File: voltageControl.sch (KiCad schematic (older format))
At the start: 5 parts

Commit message: updated with association labels
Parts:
- added C302: 100nF, symbol C
- R301: renamed from R?; value R -> 19.1K
- R302: renamed from R?; value R -> 2.2k
- gave numbers to parts that had none: 3
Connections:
- wire segments 16 -> 18
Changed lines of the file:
@@
 $EndDescr
 $Comp
-L GND #PWR?
+L GND #PWR305
 U 1 1 5521C966
 P 4500 4800
-F 0 "#PWR?" H 4500 4550 60  0001 C CNN
-F 1 "GND" H 4500 4650 60  0000 C CNN
-F 2 "" H 4500 4800 60  0000 C CNN
-F 3 "" H 4500 4800 60  0000 C CNN
-	1    4500 4800
-	1    0    0    -1
-$EndComp
-$Comp
-L GND #PWR?
+F 0 "#PWR305" H 4500 4550 60  0001 C CNN
+F 1 "GND" H 4500 4650 60  0000 C CNN
+F 2 "" H 4500 4800 60  0000 C CNN
+F 3 "" H 4500 4800 60  0000 C CNN
+	1    4500 4800
+	1    0    0    -1
+$EndComp
+$Comp
+L GND #PWR301
 U 1 1 5521C96C
 P 3700 3900
-F 0 "#PWR?" H 3700 3650 60  0001 C CNN
-F 1 "GND" H 3700 3750 60  0000 C CNN
-F 2 "" H 3700 3900 60  0000 C CNN
-F 3 "" H 3700 3900 60  0000 C CNN
-	1    3700 3900
-	1    0    0    -1
-$EndComp
-$Comp
-L GND #PWR?
+F 0 "#PWR301" H 3700 3650 60  0001 C CNN
+F 1 "GND" H 3700 3750 60  0000 C CNN
+F 2 "" H 3700 3900 60  0000 C CNN
+F 3 "" H 3700 3900 60  0000 C CNN
+	1    3700 3900
+	1    0    0    -1
+$EndComp
+$Comp
+L GND #PWR306
 U 1 1 5521C972
 P 4500 4800
-F 0 "#PWR?" H 4500 4550 60  0001 C CNN
-F 1 "GND" H 4500 4650 60  0000 C CNN
-F 2 "" H 4500 4800 60  0000 C CNN
-F 3 "" H 4500 4800 60  0000 C CNN
-	1    4500 4800
-	1    0    0    -1
-$EndComp
-$Comp
-L GND #PWR?
+F 0 "#PWR306" H 4500 4550 60  0001 C CNN
+F 1 "GND" H 4500 4650 60  0000 C CNN
+F 2 "" H 4500 4800 60  0000 C CNN
+F 3 "" H 4500 4800 60  0000 C CNN
+	1    4500 4800
+	1    0    0    -1
+$EndComp
+$Comp
+L GND #PWR302
 U 1 1 5521C978
 P 3700 3900
-F 0 "#PWR?" H 3700 3650 60  0001 C CNN
+F 0 "#PWR302" H 3700 3650 60  0001 C CNN
 F 1 "GND" H 3700 3750 60  0000 C CNN
 F 2 "" H 3700 3900 60  0000 C CNN
@@
 	4500 4700 4500 4800
 $Comp
-L GND #PWR?
+L GND #PWR307
 U 1 1 5521C982
 P 4500 4800
-F 0 "#PWR?" H 4500 4550 60  0001 C CNN
-F 1 "GND" H 4500 4650 60  0000 C CNN
-F 2 "" H 4500 4800 60  0000 C CNN
-F 3 "" H 4500 4800 60  0000 C CNN
-	1    4500 4800
-	1    0    0    -1
-$EndComp
-$Comp
-L GND #PWR?
+F 0 "#PWR307" H 4500 4550 60  0001 C CNN
+F 1 "GND" H 4500 4650 60  0000 C CNN
+F 2 "" H 4500 4800 60  0000 C CNN
+F 3 "" H 4500 4800 60  0000 C CNN
+	1    4500 4800
+	1    0    0    -1
+$EndComp
+$Comp
+L GND #PWR303
 U 1 1 5521C988
 P 3700 3900
-F 0 "#PWR?" H 3700 3650 60  0001 C CNN
-F 1 "GND" H 3700 3750 60  0000 C CNN
-F 2 "" H 3700 3900 60  0000 C CNN
-F 3 "" H 3700 3900 60  0000 C CNN
-	1    3700 3900
-	1    0    0    -1
-$EndComp
-$Comp
-L LMV358 U?
+F 0 "#PWR303" H 3700 3650 60  0001 C CNN
+F 1 "GND" H 3700 3750 60  0000 C CNN
+F 2 "" H 3700 3900 60  0000 C CNN
+F 3 "" H 3700 3900 60  0000 C CNN
+	1    3700 3900
+	1    0    0    -1
+$EndComp
+$Comp
+L LMV358 U201
 U 2 1 5521C98E
 P 4600 4300
-F 0 "U?" H 4550 4500 60  0000 L CNN
+F 0 "U201" H 4550 4500 60  0000 L CNN
 F 1 "LMV358" H 4550 4050 60  0000 L CNN
 F 2 "" H 4600 4300 60  0000 C CNN
@@
 $EndComp
 $Comp
-L GND #PWR?
+L GND #PWR308
 U 1 1 5521C995
 P 4500 4800
-F 0 "#PWR?" H 4500 4550 60  0001 C CNN
-F 1 "GND" H 4500 4650 60  0000 C CNN
-F 2 "" H 4500 4800 60  0000 C CNN
-F 3 "" H 4500 4800 60  0000 C CNN
-	1    4500 4800
-	1    0    0    -1
-$EndComp
-$Comp
-L C C?
+F 0 "#PWR308" H 4500 4550 60  0001 C CNN
+F 1 "GND" H 4500 4650 60  0000 C CNN
+F 2 "" H 4500 4800 60  0000 C CNN
+F 3 "" H 4500 4800 60  0000 C CNN
+	1    4500 4800
+	1    0    0    -1
+$EndComp
+$Comp
+L C C301
 U 1 1 5521C99B
 P 3700 3600
-F 0 "C?" H 3750 3700 50  0000 L CNN
+F 0 "C301" H 3750 3700 50  0000 L CNN
 F 1 "C" H 3750 3500 50  0000 L CNN
 F 2 "" H 3738 3450 30  0000 C CNN
@@
 $EndComp
 $Comp
-L GND #PWR?
+L GND #PWR304
 U 1 1 5521C9A2
 P 3700 3900
-F 0 "#PWR?" H 3700 3650 60  0001 C CNN
+F 0 "#PWR304" H 3700 3650 60  0001 C CNN
 F 1 "GND" H 3700 3750 60  0000 C CNN
 F 2 "" H 3700 3900 60  0000 C CNN
@@
 	5100 4300 5750 4300
 $Comp
-L DIODE D?
+L DIODE D301
 U 1 1 5521CA2B
 P 5950 4300
-F 0 "D?" H 5950 4400 50  0000 C CNN
+F 0 "D301" H 5950 4400 50  0000 C CNN
 F 1 "DIODE" H 5950 4200 50  0000 C CNN
 F 2 "" H 5950 4300 60  0000 C CNN
@@
 $EndComp
 $Comp
-L R R?
+L R R301
 U 1 1 5521CAB7
 P 7300 4900
-F 0 "R?" V 7380 4900 50  0000 C CNN
-F 1 "R" V 7307 4901 50  0000 C CNN
+F 0 "R301" V 7380 4900 50  0000 C CNN
+F 1 "19.1K" V 7307 4901 50  0000 C CNN
 F 2 "" V 7230 4900 30  0000 C CNN
 F 3 "" H 7300 4900 30  0000 C CNN
@@
 $EndComp
 $Comp
-L R R?
+L R R302
 U 1 1 5521CAFE
 P 7300 5750
-F 0 "R?" V 7380 5750 50  0000 C CNN
-F 1 "R" V 7307 5751 50  0000 C CNN
+F 0 "R302" V 7380 5750 50  0000 C CNN
+F 1 "2.2k" V 7307 5751 50  0000 C CNN
 F 2 "" V 7230 5750 30  0000 C CNN
 F 3 "" H 7300 5750 30  0000 C CNN
@@
 Wire Wire Line
 	7300 4500 7950 4500
-Text HLabel 7950 6100 2    60   Input ~ 0
+Text HLabel 8000 6250 2    60   Input ~ 0
 Current_Sink-
 Wire Wire Line
-	7300 6000 7300 6100
-Wire Wire Line
-	7300 6100 7950 6100
+	7300 6000 7300 6250
 Text HLabel 2350 4200 0    60   Input ~ 0
 DAC_Va
 Text HLabel 8000 5300 2    60   Output ~ 0
 VoltageRead
+$Comp
+L C C302
+U 1 1 55220BE7
+P 7700 5700
+F 0 "C302" H 7750 5800 50  0000 L CNN
+F 1 "100nF" H 7750 5600 50  0000 L CNN
+F 2 "" H 7738 5550 30  0000 C CNN
+F 3 "" H 7700 5700 60  0000 C CNN
+F 4 "Value" H 7700 5700 60  0001 C CNN "MPN"
+	1    7700 5700
+	1    0    0    -1
+$EndComp
+$Comp
+L GND #PWR309
+U 1 1 55220C0E
+P 7700 5950
+F 0 "#PWR309" H 7700 5700 60  0001 C CNN
+F 1 "GND" H 7700 5800 60  0000 C CNN
+F 2 "" H 7700 5950 60  0000 C CNN
+F 3 "" H 7700 5950 60  0000 C CNN
+	1    7700 5950
+	1    0    0    -1
+$EndComp
+Wire Wire Line
+	7300 6250 8000 6250
+Wire Wire Line
+	7700 5900 7700 5950
+Wire Wire Line
+	7700 5500 7700 5300
+Connection ~ 7700 5300
 $EndSCHEMATC

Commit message: updated schematic with corrected wiring after all passives became disconnected
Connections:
- wire segments 18 -> 19
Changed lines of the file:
@@
 	4100 4400 4100 5300
 Wire Wire Line
-	3700 3800 3700 3900
+	3700 3750 3700 3900
 Wire Wire Line
 	4500 4700 4500 4800
@@
 $EndComp
 Wire Wire Line
-	7300 5150 7300 5500
+	7300 5050 7300 5600
 Connection ~ 7300 5300
 Text HLabel 7950 4300 2    60   Output ~ 0
@@
 Current_Sink+
 Wire Wire Line
-	7300 4650 7300 4500
+	7300 4500 7300 4750
 Wire Wire Line
 	7300 4500 7950 4500
@@
 Current_Sink-
 Wire Wire Line
-	7300 6000 7300 6250
+	7300 5900 7300 6250
 Text HLabel 2350 4200 0    60   Input ~ 0
 DAC_Va
@@
 	7300 6250 8000 6250
 Wire Wire Line
-	7700 5900 7700 5950
+	7700 5850 7700 5950
 Wire Wire Line
-	7700 5500 7700 5300
+	7700 5300 7700 5550
 Connection ~ 7700 5300
+Wire Wire Line
+	3700 3450 3700 3400
+Connection ~ 3700 3400
 $EndSCHEMATC

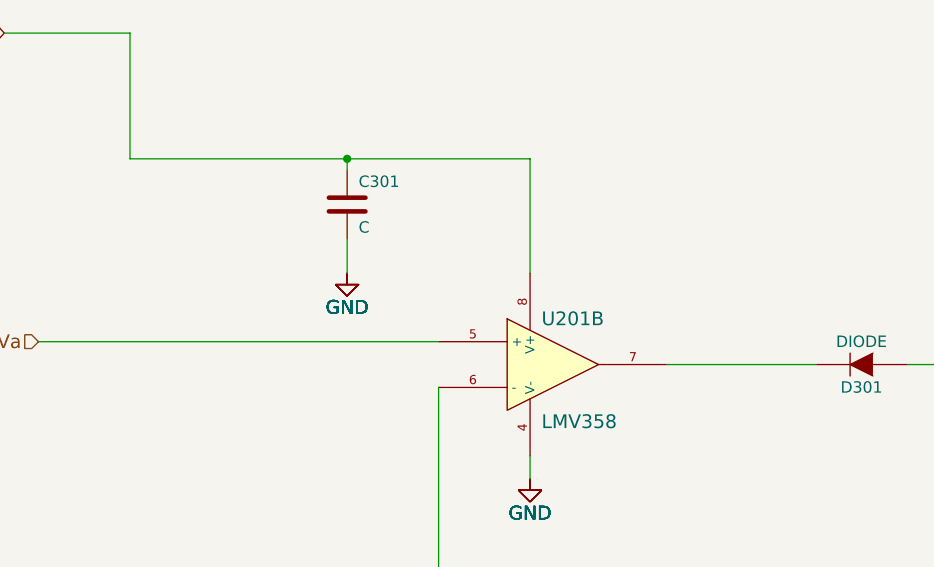
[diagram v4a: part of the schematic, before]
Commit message: updated project with most footprint associations
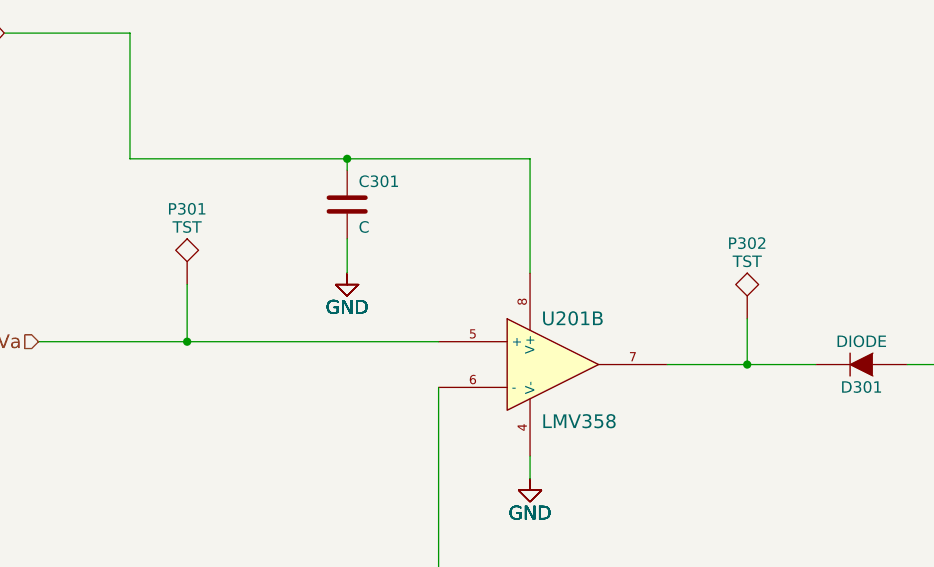
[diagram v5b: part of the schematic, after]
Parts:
- added P301, P302: TST, symbol TST
- C301, C302: footprint (none) -> Capacitors_SMD:C_0805_HandSoldering
- R301, R302: footprint (none) -> Resistors_SMD:R_0805_HandSoldering
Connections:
- net DAC_Va: now also P301.1
- net at D301.2 (K), U201.7: now also P302.1
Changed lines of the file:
@@
 $EndDescr
 $Comp
-L GND #PWR013
+L GND #PWR305
 U 1 1 5521C966
 P 4500 4800
-F 0 "#PWR013" H 4500 4550 60  0001 C CNN
-F 1 "GND" H 4500 4650 60  0000 C CNN
-F 2 "" H 4500 4800 60  0000 C CNN
-F 3 "" H 4500 4800 60  0000 C CNN
-	1    4500 4800
-	1    0    0    -1
-$EndComp
-$Comp
-L GND #PWR014
+F 0 "#PWR305" H 4500 4550 60  0001 C CNN
+F 1 "GND" H 4500 4650 60  0000 C CNN
+F 2 "" H 4500 4800 60  0000 C CNN
+F 3 "" H 4500 4800 60  0000 C CNN
+	1    4500 4800
+	1    0    0    -1
+$EndComp
+$Comp
+L GND #PWR301
 U 1 1 5521C96C
 P 3700 3900
-F 0 "#PWR014" H 3700 3650 60  0001 C CNN
-F 1 "GND" H 3700 3750 60  0000 C CNN
-F 2 "" H 3700 3900 60  0000 C CNN
-F 3 "" H 3700 3900 60  0000 C CNN
-	1    3700 3900
-	1    0    0    -1
-$EndComp
-$Comp
-L GND #PWR015
+F 0 "#PWR301" H 3700 3650 60  0001 C CNN
+F 1 "GND" H 3700 3750 60  0000 C CNN
+F 2 "" H 3700 3900 60  0000 C CNN
+F 3 "" H 3700 3900 60  0000 C CNN
+	1    3700 3900
+	1    0    0    -1
+$EndComp
+$Comp
+L GND #PWR306
 U 1 1 5521C972
 P 4500 4800
-F 0 "#PWR015" H 4500 4550 60  0001 C CNN
-F 1 "GND" H 4500 4650 60  0000 C CNN
-F 2 "" H 4500 4800 60  0000 C CNN
-F 3 "" H 4500 4800 60  0000 C CNN
-	1    4500 4800
-	1    0    0    -1
-$EndComp
-$Comp
-L GND #PWR016
+F 0 "#PWR306" H 4500 4550 60  0001 C CNN
+F 1 "GND" H 4500 4650 60  0000 C CNN
+F 2 "" H 4500 4800 60  0000 C CNN
+F 3 "" H 4500 4800 60  0000 C CNN
+	1    4500 4800
+	1    0    0    -1
+$EndComp
+$Comp
+L GND #PWR302
 U 1 1 5521C978
 P 3700 3900
-F 0 "#PWR016" H 3700 3650 60  0001 C CNN
-F 1 "GND" H 3700 3750 60  0000 C CNN
-F 2 "" H 3700 3900 60  0000 C CNN
-F 3 "" H 3700 3900 60  0000 C CNN
-	1    3700 3900
-	1    0    0    -1
-$EndComp
-Wire Wire Line
-	4100 5300 8000 5300
-Wire Wire Line
-	4100 4400 4100 5300
-Wire Wire Line
-	3700 3750 3700 3900
-Wire Wire Line
-	4500 4700 4500 4800
-$Comp
-L GND #PWR017
+F 0 "#PWR302" H 3700 3650 60  0001 C CNN
+F 1 "GND" H 3700 3750 60  0000 C CNN
+F 2 "" H 3700 3900 60  0000 C CNN
+F 3 "" H 3700 3900 60  0000 C CNN
+	1    3700 3900
+	1    0    0    -1
+$EndComp
+$Comp
+L GND #PWR307
 U 1 1 5521C982
 P 4500 4800
-F 0 "#PWR017" H 4500 4550 60  0001 C CNN
-F 1 "GND" H 4500 4650 60  0000 C CNN
-F 2 "" H 4500 4800 60  0000 C CNN
-F 3 "" H 4500 4800 60  0000 C CNN
-	1    4500 4800
-	1    0    0    -1
-$EndComp
-$Comp
-L GND #PWR018
+F 0 "#PWR307" H 4500 4550 60  0001 C CNN
+F 1 "GND" H 4500 4650 60  0000 C CNN
+F 2 "" H 4500 4800 60  0000 C CNN
+F 3 "" H 4500 4800 60  0000 C CNN
+	1    4500 4800
+	1    0    0    -1
+$EndComp
+$Comp
+L GND #PWR303
 U 1 1 5521C988
 P 3700 3900
-F 0 "#PWR018" H 3700 3650 60  0001 C CNN
+F 0 "#PWR303" H 3700 3650 60  0001 C CNN
 F 1 "GND" H 3700 3750 60  0000 C CNN
 F 2 "" H 3700 3900 60  0000 C CNN
@@
 F 0 "U201" H 4550 4500 60  0000 L CNN
 F 1 "LMV358" H 4550 4050 60  0000 L CNN
-F 2 "" H 4600 4300 60  0000 C CNN
+F 2 "" H 4600 4300 60  0001 C CNN
 F 3 "" H 4600 4300 60  0000 C CNN
 	2    4600 4300
@@
 $EndComp
 $Comp
-L GND #PWR019
+L GND #PWR308
 U 1 1 5521C995
 P 4500 4800
-F 0 "#PWR019" H 4500 4550 60  0001 C CNN
+F 0 "#PWR308" H 4500 4550 60  0001 C CNN
 F 1 "GND" H 4500 4650 60  0000 C CNN
 F 2 "" H 4500 4800 60  0000 C CNN
@@
 F 0 "C301" H 3750 3700 50  0000 L CNN
 F 1 "C" H 3750 3500 50  0000 L CNN
-F 2 "" H 3738 3450 30  0000 C CNN
+F 2 "Capacitors_SMD:C_0805_HandSoldering" H 3738 3450 30  0001 C CNN
 F 3 "" H 3700 3600 60  0000 C CNN
 	1    3700 3600
@@
 $EndComp
 $Comp
-L GND #PWR020
+L GND #PWR304
 U 1 1 5521C9A2
 P 3700 3900
-F 0 "#PWR020" H 3700 3650 60  0001 C CNN
+F 0 "#PWR304" H 3700 3650 60  0001 C CNN
 F 1 "GND" H 3700 3750 60  0000 C CNN
 F 2 "" H 3700 3900 60  0000 C CNN
@@
 Text GLabel 2200 2850 0    60   Input ~ 0
 2.7V
-Wire Wire Line
-	4500 3900 4500 3400
-Wire Wire Line
-	4500 3400 2750 3400
-Wire Wire Line
-	2750 3400 2750 2850
-Wire Wire Line
-	2750 2850 2200 2850
-Wire Wire Line
-	2350 4200 4100 4200
-Wire Wire Line
-	5100 4300 5750 4300
 $Comp
 L DIODE D301
@@
 F 0 "D301" H 5950 4400 50  0000 C CNN
 F 1 "DIODE" H 5950 4200 50  0000 C CNN
-F 2 "" H 5950 4300 60  0000 C CNN
+F 2 "" H 5950 4300 60  0001 C CNN
 F 3 "" H 5950 4300 60  0000 C CNN
 	1    5950 4300
@@
 F 0 "R301" V 7380 4900 50  0000 C CNN
 F 1 "19.1K" V 7307 4901 50  0000 C CNN
-F 2 "" V 7230 4900 30  0000 C CNN
+F 2 "Resistors_SMD:R_0805_HandSoldering" V 7230 4900 30  0001 C CNN
 F 3 "" H 7300 4900 30  0000 C CNN
 	1    7300 4900
@@
 F 0 "R302" V 7380 5750 50  0000 C CNN
 F 1 "2.2k" V 7307 5751 50  0000 C CNN
-F 2 "" V 7230 5750 30  0000 C CNN
+F 2 "Resistors_SMD:R_0805_HandSoldering" V 7230 5750 30  0001 C CNN
 F 3 "" H 7300 5750 30  0000 C CNN
 	1    7300 5750
 	1    0    0    -1
 $EndComp
-Wire Wire Line
-	7300 5050 7300 5600
-Connection ~ 7300 5300
 Text HLabel 7950 4300 2    60   Output ~ 0
 Vcontrol
-Wire Wire Line
-	6150 4300 7950 4300
 Text HLabel 7950 4500 2    60   Input ~ 0
 Current_Sink+
-Wire Wire Line
-	7300 4500 7300 4750
-Wire Wire Line
-	7300 4500 7950 4500
 Text HLabel 8000 6250 2    60   Input ~ 0
 Current_Sink-
-Wire Wire Line
-	7300 5900 7300 6250
 Text HLabel 2350 4200 0    60   Input ~ 0
 DAC_Va
@@
 F 0 "C302" H 7750 5800 50  0000 L CNN
 F 1 "100nF" H 7750 5600 50  0000 L CNN
-F 2 "" H 7738 5550 30  0000 C CNN
+F 2 "Capacitors_SMD:C_0805_HandSoldering" H 7738 5550 30  0001 C CNN
 F 3 "" H 7700 5700 60  0000 C CNN
 F 4 "Value" H 7700 5700 60  0001 C CNN "MPN"
@@
 $EndComp
 $Comp
-L GND #PWR021
+L GND #PWR309
 U 1 1 55220C0E
 P 7700 5950
-F 0 "#PWR021" H 7700 5700 60  0001 C CNN
+F 0 "#PWR309" H 7700 5700 60  0001 C CNN
 F 1 "GND" H 7700 5800 60  0000 C CNN
 F 2 "" H 7700 5950 60  0000 C CNN
@@
 	1    0    0    -1
 $EndComp
+$Comp
+L TST P301
+U 1 1 5528F0BE
+P 3000 3950
+F 0 "P301" H 3000 4250 50  0000 C BNN
+F 1 "TST" H 3000 4200 50  0000 C CNN
+F 2 "" H 3000 3950 60  0000 C CNN
+F 3 "" H 3000 3950 60  0000 C CNN
+	1    3000 3950
+	1    0    0    -1
+$EndComp
+Wire Wire Line
+	4100 5300 8000 5300
+Wire Wire Line
+	4100 4400 4100 5300
+Wire Wire Line
+	3700 3750 3700 3900
+Wire Wire Line
+	4500 4700 4500 4800
+Wire Wire Line
+	4500 3900 4500 3400
+Wire Wire Line
+	4500 3400 2750 3400
+Wire Wire Line
+	2750 3400 2750 2850
+Wire Wire Line
+	2750 2850 2200 2850
+Wire Wire Line
+	2350 4200 4100 4200
+Wire Wire Line
+	5100 4300 5750 4300
+Wire Wire Line
+	7300 5050 7300 5600
+Connection ~ 7300 5300
+Wire Wire Line
+	6150 4300 7950 4300
+Wire Wire Line
+	7300 4500 7300 4750
+Wire Wire Line
+	7300 4500 7950 4500
+Wire Wire Line
+	7300 5900 7300 6250
 Wire Wire Line
 	7300 6250 8000 6250
@@
 	3700 3450 3700 3400
 Connection ~ 3700 3400
+Wire Wire Line
+	3000 3950 3000 4200
+Connection ~ 3000 4200
+$Comp
+L TST P302
+U 1 1 5528F58F
+P 5450 4100
+F 0 "P302" H 5450 4400 50  0000 C BNN
+F 1 "TST" H 5450 4350 50  0000 C CNN
+F 2 "" H 5450 4100 60  0000 C CNN
+F 3 "" H 5450 4100 60  0000 C CNN
+	1    5450 4100
+	1    0    0    -1
+$EndComp
+Wire Wire Line
+	5450 4100 5450 4300
+Connection ~ 5450 4300
 $EndSCHEMATC

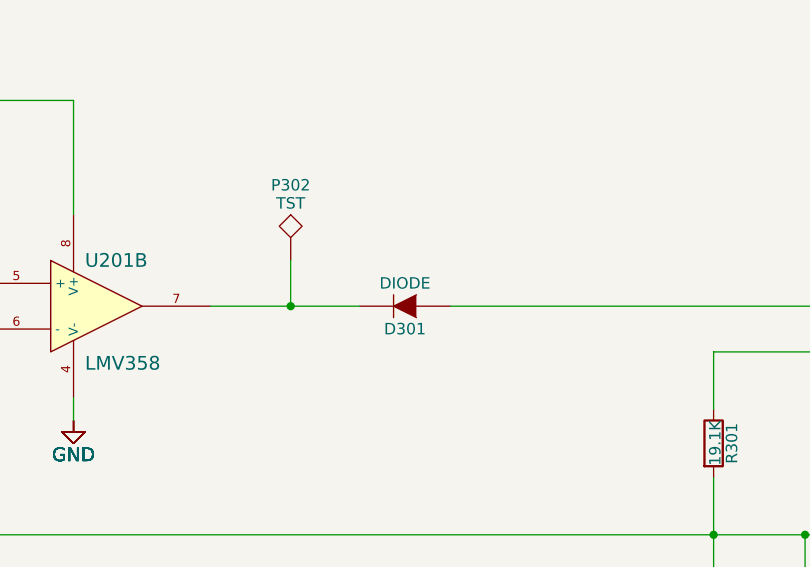
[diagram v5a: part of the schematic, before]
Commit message: association of footprints complete
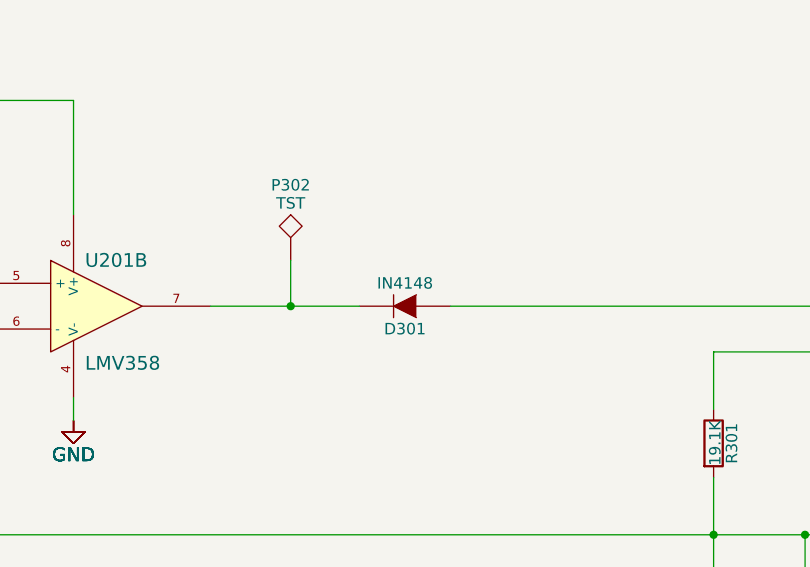
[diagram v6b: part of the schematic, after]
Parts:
- D301: value DIODE -> IN4148; footprint (none) -> SMD_Packages:SOD-523; MPN (none) -> 1N4148WT-7
- P301, P302: footprint (none) -> Measurement_Points:Measurement_Point_Round-TH_Small
- U201: footprint (none) -> SMD_Packages:SOIC-8-N
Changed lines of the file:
@@
 $EndDescr
 $Comp
-L GND #PWR305
+L GND #PWR013
 U 1 1 5521C966
 P 4500 4800
-F 0 "#PWR305" H 4500 4550 60  0001 C CNN
-F 1 "GND" H 4500 4650 60  0000 C CNN
-F 2 "" H 4500 4800 60  0000 C CNN
-F 3 "" H 4500 4800 60  0000 C CNN
-	1    4500 4800
-	1    0    0    -1
-$EndComp
-$Comp
-L GND #PWR301
+F 0 "#PWR013" H 4500 4550 60  0001 C CNN
+F 1 "GND" H 4500 4650 60  0000 C CNN
+F 2 "" H 4500 4800 60  0000 C CNN
+F 3 "" H 4500 4800 60  0000 C CNN
+	1    4500 4800
+	1    0    0    -1
+$EndComp
+$Comp
+L GND #PWR014
 U 1 1 5521C96C
 P 3700 3900
-F 0 "#PWR301" H 3700 3650 60  0001 C CNN
-F 1 "GND" H 3700 3750 60  0000 C CNN
-F 2 "" H 3700 3900 60  0000 C CNN
-F 3 "" H 3700 3900 60  0000 C CNN
-	1    3700 3900
-	1    0    0    -1
-$EndComp
-$Comp
-L GND #PWR306
+F 0 "#PWR014" H 3700 3650 60  0001 C CNN
+F 1 "GND" H 3700 3750 60  0000 C CNN
+F 2 "" H 3700 3900 60  0000 C CNN
+F 3 "" H 3700 3900 60  0000 C CNN
+	1    3700 3900
+	1    0    0    -1
+$EndComp
+$Comp
+L GND #PWR015
 U 1 1 5521C972
 P 4500 4800
-F 0 "#PWR306" H 4500 4550 60  0001 C CNN
-F 1 "GND" H 4500 4650 60  0000 C CNN
-F 2 "" H 4500 4800 60  0000 C CNN
-F 3 "" H 4500 4800 60  0000 C CNN
-	1    4500 4800
-	1    0    0    -1
-$EndComp
-$Comp
-L GND #PWR302
+F 0 "#PWR015" H 4500 4550 60  0001 C CNN
+F 1 "GND" H 4500 4650 60  0000 C CNN
+F 2 "" H 4500 4800 60  0000 C CNN
+F 3 "" H 4500 4800 60  0000 C CNN
+	1    4500 4800
+	1    0    0    -1
+$EndComp
+$Comp
+L GND #PWR016
 U 1 1 5521C978
 P 3700 3900
-F 0 "#PWR302" H 3700 3650 60  0001 C CNN
-F 1 "GND" H 3700 3750 60  0000 C CNN
-F 2 "" H 3700 3900 60  0000 C CNN
-F 3 "" H 3700 3900 60  0000 C CNN
-	1    3700 3900
-	1    0    0    -1
-$EndComp
-$Comp
-L GND #PWR307
+F 0 "#PWR016" H 3700 3650 60  0001 C CNN
+F 1 "GND" H 3700 3750 60  0000 C CNN
+F 2 "" H 3700 3900 60  0000 C CNN
+F 3 "" H 3700 3900 60  0000 C CNN
+	1    3700 3900
+	1    0    0    -1
+$EndComp
+$Comp
+L GND #PWR017
 U 1 1 5521C982
 P 4500 4800
-F 0 "#PWR307" H 4500 4550 60  0001 C CNN
-F 1 "GND" H 4500 4650 60  0000 C CNN
-F 2 "" H 4500 4800 60  0000 C CNN
-F 3 "" H 4500 4800 60  0000 C CNN
-	1    4500 4800
-	1    0    0    -1
-$EndComp
-$Comp
-L GND #PWR303
+F 0 "#PWR017" H 4500 4550 60  0001 C CNN
+F 1 "GND" H 4500 4650 60  0000 C CNN
+F 2 "" H 4500 4800 60  0000 C CNN
+F 3 "" H 4500 4800 60  0000 C CNN
+	1    4500 4800
+	1    0    0    -1
+$EndComp
+$Comp
+L GND #PWR018
 U 1 1 5521C988
 P 3700 3900
-F 0 "#PWR303" H 3700 3650 60  0001 C CNN
+F 0 "#PWR018" H 3700 3650 60  0001 C CNN
 F 1 "GND" H 3700 3750 60  0000 C CNN
 F 2 "" H 3700 3900 60  0000 C CNN
@@
 F 0 "U201" H 4550 4500 60  0000 L CNN
 F 1 "LMV358" H 4550 4050 60  0000 L CNN
-F 2 "" H 4600 4300 60  0001 C CNN
+F 2 "SMD_Packages:SOIC-8-N" H 4600 4300 60  0001 C CNN
 F 3 "" H 4600 4300 60  0000 C CNN
 	2    4600 4300
@@
 $EndComp
 $Comp
-L GND #PWR308
+L GND #PWR019
 U 1 1 5521C995
 P 4500 4800
-F 0 "#PWR308" H 4500 4550 60  0001 C CNN
+F 0 "#PWR019" H 4500 4550 60  0001 C CNN
 F 1 "GND" H 4500 4650 60  0000 C CNN
 F 2 "" H 4500 4800 60  0000 C CNN
@@
 $EndComp
 $Comp
-L GND #PWR304
+L GND #PWR020
 U 1 1 5521C9A2
 P 3700 3900
-F 0 "#PWR304" H 3700 3650 60  0001 C CNN
+F 0 "#PWR020" H 3700 3650 60  0001 C CNN
 F 1 "GND" H 3700 3750 60  0000 C CNN
 F 2 "" H 3700 3900 60  0000 C CNN
@@
 P 5950 4300
 F 0 "D301" H 5950 4400 50  0000 C CNN
-F 1 "DIODE" H 5950 4200 50  0000 C CNN
-F 2 "" H 5950 4300 60  0001 C CNN
-F 3 "" H 5950 4300 60  0000 C CNN
+F 1 "IN4148" H 5950 4200 50  0000 C CNN
+F 2 "SMD_Packages:SOD-523" H 5950 4300 60  0001 C CNN
+F 3 "http://www.diodes.com/datasheets/ds30396.pdf" H 5950 4300 60  0001 C CNN
+F 4 "1N4148WT-7" H 5950 4300 60  0001 C CNN "MPN"
 	1    5950 4300
 	-1   0    0    1
@@
 $EndComp
 $Comp
-L GND #PWR309
+L GND #PWR021
 U 1 1 55220C0E
 P 7700 5950
-F 0 "#PWR309" H 7700 5700 60  0001 C CNN
+F 0 "#PWR021" H 7700 5700 60  0001 C CNN
 F 1 "GND" H 7700 5800 60  0000 C CNN
 F 2 "" H 7700 5950 60  0000 C CNN
@@
 F 0 "P301" H 3000 4250 50  0000 C BNN
 F 1 "TST" H 3000 4200 50  0000 C CNN
-F 2 "" H 3000 3950 60  0000 C CNN
+F 2 "Measurement_Points:Measurement_Point_Round-TH_Small" H 3000 3950 60  0001 C CNN
 F 3 "" H 3000 3950 60  0000 C CNN
 	1    3000 3950
@@
 F 0 "P302" H 5450 4400 50  0000 C BNN
 F 1 "TST" H 5450 4350 50  0000 C CNN
-F 2 "" H 5450 4100 60  0000 C CNN
+F 2 "Measurement_Points:Measurement_Point_Round-TH_Small" H 5450 4100 60  0001 C CNN
 F 3 "" H 5450 4100 60  0000 C CNN
 	1    5450 4100
